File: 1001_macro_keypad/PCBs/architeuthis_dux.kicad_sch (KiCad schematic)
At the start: 18 parts, among them J1 ePaperModule, J2 RotaryModule_01, J3 RotaryModule_02, SW01 MX_SW, SW10 MX_SW, SW11 MX_SW, SW12 MX_SW, SW13 MX_SW, SW14 MX_SW, SW2 MX_SW, SW3 MX_SW, SW4 MX_SW, SW5 MX_SW, SW6 MX_SW, SW7 MX_SW, SW8 MX_SW, SW9 MX_SW, U1 Pico

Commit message: pcb modify
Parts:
- added D1: 1N4148, Diode_THT:D_DO-35_SOD27_P7.62mm_Horizontal, symbol Diode:1N4148
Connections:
- net SW6: now reaches SW6.1
- net at SW01.1: now also D1.2 (A)
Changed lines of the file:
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@@
     (stroke (width 0) (type default))
+  )
+  (global_label "SW6" (shape input) (at 57.15 73.66 90) (fields_autoplaced)
+    (effects (font (size 1.27 1.27)) (justify left))
+    (property "Intersheetrefs" "${INTERSHEET_REFS}" (at 57.15 66.8838 90)
+      (effects (font (size 1.27 1.27)) (justify left) hide)
+    )
   )
   (symbol (lib_id "Switch:SW_Push_45deg") (at 76.2 59.69 0) (unit 1)
@@
         )
       )
+    )
+  )
+  (symbol (lib_id "Diode:1N4148") (at 38.1 57.15 0) (unit 1)
+    (in_bom yes) (on_board yes) (dnp no) (fields_autoplaced)
+    (property "Reference" "D1" (at 38.1 52.07 0)
+      (effects (font (size 1.27 1.27)))
+    )
+    (property "Value" "1N4148" (at 38.1 54.61 0)
+      (effects (font (size 1.27 1.27)))
+    )
+    (property "Footprint" "Diode_THT:D_DO-35_SOD27_P7.62mm_Horizontal" (at 38.1 57.15 0)
+      (effects (font (size 1.27 1.27)) hide)
+    )
+    (property "Datasheet" "https://assets.nexperia.com/documents/data-sheet/1N4148_1N4448.pdf" (at 38.1 57.15 0)
+      (effects (font (size 1.27 1.27)) hide)
+    )
+    (property "Sim.Device" "D" (at 38.1 57.15 0)
+      (effects (font (size 1.27 1.27)) hide)
+    )
+    (property "Sim.Pins" "1=K 2=A" (at 38.1 57.15 0)
+      (effects (font (size 1.27 1.27)) hide)
+    )
+    (pin "1")
+    (pin "2")
+    (instances
+      (project "architeuthis_dux"
+        (path "/4d2fbfb9-c67d-4ccb-bbaa-2d2f4be0cbd8"
+          (reference "D1") (unit 1)
+        )
+      )

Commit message: 배션중
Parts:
- added D10, D11, D12, D13, D14, D2, D3, D4, D5, D6, D7, D8, D9: 1N4148, Diode_THT:D_DO-35_SOD27_P7.62mm_Horizontal, symbol Diode:1N4148
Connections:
- net GND: no longer SW01.2, SW10.2, SW11.2, SW12.2, SW13.2, SW14.2, SW2.2, SW3.2, SW4.2, SW5.2, SW6.2, SW7.2, SW8.2, SW9.2
- net at SW3.1: now also D3.2 (A)
- net at SW8.1: now also D8.2 (A)
- net at SW11.1: now also D11.2 (A)
- net at SW2.1: now also D2.2 (A)
- net at SW14.1: now also D14.2 (A)
- net at SW13.1: now also D13.2 (A)
- net at SW9.1: now also D9.2 (A)
- net at SW5.1: now also D5.2 (A)
- net ROW0: now reaches D1.1 (K)
- net ROW0: now also U1.1 (GPIO0), D2.1 (K), D3.1 (K), D4.1 (K)
- net COL2: now reaches U1.10 (GPIO7)
- net COL2: now also SW11.2, SW13.2, SW3.2, SW7.2
- net ROW1: now reaches U1.2 (GPIO1)
- net ROW1: now also D5.1 (K), D6.1 (K), D7.1 (K), D8.1 (K)
- net ROW2: now reaches U1.4 (GPIO2)
- net ROW2: now also D10.1 (K), D11.1 (K), D12.1 (K), D9.1 (K)
- net ROW3: now reaches U1.5 (GPIO3)
- net ROW3: now also D13.1 (K), D14.1 (K)
- net COL1: now reaches U1.6 (GPIO4)
- net COL1: now also SW10.2, SW2.2, SW6.2
- net COL0: now reaches U1.7 (GPIO5)
- net COL0: now also SW01.2, SW5.2, SW9.2
- net COL3: now reaches U1.9 (GPIO6)
- net COL3: now also SW12.2, SW14.2, SW4.2, SW8.2
- net at SW7.1: now also D7.2 (A)
- net at SW12.1: now also D12.2 (A)
- net at SW10.1: now also D10.2 (A)
- net at SW4.1: now also D4.2 (A)
- net SW6: no longer names the net of SW6.1
- net SW6: now also D6.2 (A)
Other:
- moved on the sheet: D1, SW01, SW10, SW11, SW12, SW13, SW14, SW2, SW3, SW4, SW5, SW6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

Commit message: 재배선
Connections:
- net COL0: now also SW12.2, SW4.2, SW8.2, U1.6 (GPIO4); no longer SW01.2, SW5.2, SW9.2, U1.7 (GPIO5)
- net COL1: now also SW11.2, SW3.2, SW7.2, U1.7 (GPIO5); no longer SW10.2, SW2.2, SW6.2, U1.6 (GPIO4)
- net COL2: now also SW01.2, SW14.2, SW5.2, SW9.2, U1.9 (GPIO6); no longer SW11.2, SW13.2, SW3.2, SW7.2, U1.10 (GPIO7)
- net COL3: now also SW10.2, SW13.2, SW2.2, SW6.2, U1.10 (GPIO7); no longer SW12.2, SW14.2, SW4.2, SW8.2, U1.9 (GPIO6)
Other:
- moved on the sheet: D13, D14, SW13, SW14

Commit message: ePaper
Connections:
- net GND: now also J1.7 (GND), J2.5 (GND), J3.5 (Pin_5)
- net +5V: now reaches J1.8 (VCC)
- net +5V: now also J2.1 (5V), J3.1 (Pin_1), U1.40 (VBUS)
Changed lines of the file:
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@@
+    )
+  )
+  (symbol (lib_id "power:+5V") (at 175.26 92.71 90) (unit 1)
+    (in_bom yes) (on_board yes) (dnp no) (fields_autoplaced)
+    (property "Reference" "#PWR04" (at 179.07 92.71 0)
+      (effects (font (size 1.27 1.27)) hide)
+    )
+    (property "Value" "+5V" (at 171.45 93.345 90)
+      (effects (font (size 1.27 1.27)) (justify left))
+    )
+    (property "Footprint" "" (at 175.26 92.71 0)
+      (effects (font (size 1.27 1.27)) hide)
+    )
+    (property "Datasheet" "" (at 175.26 92.71 0)
+      (effects (font (size 1.27 1.27)) hide)
+    )
+    (pin "1")
+    (instances
+      (project "architeuthis_dux"
+        (path "/4d2fbfb9-c67d-4ccb-bbaa-2d2f4be0cbd8"
+          (reference "#PWR04") (unit 1)
+        )
+      )
     )
   )
@@
     )
   )
-  (symbol (lib_id "Connector_Generic:Conn_01x05") (at 180.34 82.55 0) (unit 1)
+  (symbol (lib_name "Conn_01x05_1") (lib_id "Connector_Generic:Conn_01x05") (at 180.34 82.55 0) (unit 1)
     (in_bom yes) (on_board yes) (dnp no) (fields_autoplaced)
     (property "Reference" "J2" (at 182.88 81.915 0)
@@
     )
   )
+  (symbol (lib_id "power:GND") (at 208.28 92.71 270) (unit 1)
+    (in_bom yes) (on_board yes) (dnp no) (fields_autoplaced)
+    (property "Reference" "#PWR014" (at 201.93 92.71 0)
+      (effects (font (size 1.27 1.27)) hide)
+    )
+    (property "Value" "GND" (at 204.47 93.345 90)
+      (effects (font (size 1.27 1.27)) (justify right))
+    )
+    (property "Footprint" "" (at 208.28 92.71 0)
+      (effects (font (size 1.27 1.27)) hide)
+    )
+    (property "Datasheet" "" (at 208.28 92.71 0)
+      (effects (font (size 1.27 1.27)) hide)
+    )
+    (pin "1")
+    (instances
+      (project "architeuthis_dux"
+        (path "/4d2fbfb9-c67d-4ccb-bbaa-2d2f4be0cbd8"
+          (reference "#PWR014") (unit 1)
+        )
+      )
+    )
+  )
+  (symbol (lib_id "power:+5V") (at 175.26 77.47 90) (unit 1)
+    (in_bom yes) (on_board yes) (dnp no) (fields_autoplaced)
+    (property "Reference" "#PWR03" (at 179.07 77.47 0)
+      (effects (font (size 1.27 1.27)) hide)
+    )
+    (property "Value" "+5V" (at 171.45 78.105 90)
+      (effects (font (size 1.27 1.27)) (justify left))
+    )
+    (property "Footprint" "" (at 175.26 77.47 0)
+      (effects (font (size 1.27 1.27)) hide)
+    )
+    (property "Datasheet" "" (at 175.26 77.47 0)
+      (effects (font (size 1.27 1.27)) hide)
+    )
+    (pin "1")
+    (instances
+      (project "architeuthis_dux"
+        (path "/4d2fbfb9-c67d-4ccb-bbaa-2d2f4be0cbd8"
+          (reference "#PWR03") (unit 1)
+        )
+      )
+    )
+  )
+  (symbol (lib_id "power:GND") (at 175.26 87.63 270) (unit 1)
+    (in_bom yes) (on_board yes) (dnp no) (fields_autoplaced)
+    (property "Reference" "#PWR012" (at 168.91 87.63 0)
+      (effects (font (size 1.27 1.27)) hide)
+    )
+    (property "Value" "GND" (at 171.45 88.265 90)
+      (effects (font (size 1.27 1.27)) (justify right))
+    )
+    (property "Footprint" "" (at 175.26 87.63 0)
+      (effects (font (size 1.27 1.27)) hide)
+    )
+    (property "Datasheet" "" (at 175.26 87.63 0)
+      (effects (font (size 1.27 1.27)) hide)
+    )
+    (pin "1")
+    (instances
+      (project "architeuthis_dux"
+        (path "/4d2fbfb9-c67d-4ccb-bbaa-2d2f4be0cbd8"
+          (reference "#PWR012") (unit 1)
+        )
+      )
+    )
+  )
   (symbol (lib_id "Switch:SW_Push_45deg") (at 35.56 91.44 0) (unit 1)
     (in_bom yes) (on_board yes) (dnp no) (fields_autoplaced)
@@
         (path "/4d2fbfb9-c67d-4ccb-bbaa-2d2f4be0cbd8"
           (reference "D1") (unit 1)
+        )
+      )
+    )
+  )
+  (symbol (lib_id "power:+5V") (at 151.13 41.91 270) (unit 1)
+    (in_bom yes) (on_board yes) (dnp no) (fields_autoplaced)
+    (property "Reference" "#PWR01" (at 147.32 41.91 0)
+      (effects (font (size 1.27 1.27)) hide)
+    )
+    (property "Value" "+5V" (at 154.94 42.545 90)
+      (effects (font (size 1.27 1.27)) (justify left))
+    )
+    (property "Footprint" "" (at 151.13 41.91 0)
+      (effects (font (size 1.27 1.27)) hide)
+    )
+    (property "Datasheet" "" (at 151.13 41.91 0)
+      (effects (font (size 1.27 1.27)) hide)
+    )
+    (pin "1")
+    (instances
+      (project "architeuthis_dux"
+        (path "/4d2fbfb9-c67d-4ccb-bbaa-2d2f4be0cbd8"
+          (reference "#PWR01") (unit 1)
         )
       )
@@
     )
   )
+  (symbol (lib_id "power:GND") (at 175.26 102.87 270) (unit 1)
+    (in_bom yes) (on_board yes) (dnp no) (fields_autoplaced)
+    (property "Reference" "#PWR013" (at 168.91 102.87 0)
+      (effects (font (size 1.27 1.27)) hide)
+    )
+    (property "Value" "GND" (at 171.45 103.505 90)
+      (effects (font (size 1.27 1.27)) (justify right))
+    )
+    (property "Footprint" "" (at 175.26 102.87 0)
+      (effects (font (size 1.27 1.27)) hide)
+    )
+    (property "Datasheet" "" (at 175.26 102.87 0)
+      (effects (font (size 1.27 1.27)) hide)
+    )
+    (pin "1")
+    (instances
+      (project "architeuthis_dux"
+        (path "/4d2fbfb9-c67d-4ccb-bbaa-2d2f4be0cbd8"
+          (reference "#PWR013") (unit 1)
+        )
+      )
+    )
+  )
   (symbol (lib_id "power:GND") (at 151.13 46.99 90) (unit 1)
     (in_bom yes) (on_board yes) (dnp no) (fields_autoplaced)
@@
         )
       )
+    )
+  )
+  (symbol (lib_id "power:+5V") (at 208.28 95.25 90) (unit 1)
+    (in_bom yes) (on_board yes) (dnp no) (fields_autoplaced)
+    (property "Reference" "#PWR02" (at 212.09 95.25 0)
+      (effects (font (size 1.27 1.27)) hide)
+    )
+    (property "Value" "+5V" (at 204.47 95.885 90)
+      (effects (font (size 1.27 1.27)) (justify left))
+    )
+    (property "Footprint" "" (at 208.28 95.25 0)
+      (effects (font (size 1.27 1.27)) hide)
+    )
+    (property "Datasheet" "" (at 208.28 95.25 0)
+      (effects (font (size 1.27 1.27)) hide)
+    )
+    (pin "1")
+    (instances
+      (project "architeuthis_dux"
+        (path "/4d2fbfb9-c67d-4ccb-bbaa-2d2f4be0cbd8"
+          (reference "#PWR02") (unit 1)
+        )
+      )

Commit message: 일부수정
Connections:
- net +5V: now also J1.1 (BUSY); no longer J1.8 (VCC)
- net GND: now also J1.2 (RES); no longer J1.7 (GND)
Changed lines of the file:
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@@
     )
   )
-  (symbol (lib_id "power:GND") (at 208.28 92.71 270) (unit 1)
-    (in_bom yes) (on_board yes) (dnp no) (fields_autoplaced)
-    (property "Reference" "#PWR014" (at 201.93 92.71 0)
-      (effects (font (size 1.27 1.27)) hide)
-    )
-    (property "Value" "GND" (at 204.47 93.345 90)
+  (symbol (lib_id "power:GND") (at 208.28 80.01 270) (unit 1)
+    (in_bom yes) (on_board yes) (dnp no) (fields_autoplaced)
+    (property "Reference" "#PWR014" (at 201.93 80.01 0)
+      (effects (font (size 1.27 1.27)) hide)
+    )
+    (property "Value" "GND" (at 204.47 80.645 90)
       (effects (font (size 1.27 1.27)) (justify right))
     )
-    (property "Footprint" "" (at 208.28 92.71 0)
-      (effects (font (size 1.27 1.27)) hide)
-    )
-    (property "Datasheet" "" (at 208.28 92.71 0)
+    (property "Footprint" "" (at 208.28 80.01 0)
+      (effects (font (size 1.27 1.27)) hide)
+    )
+    (property "Datasheet" "" (at 208.28 80.01 0)
       (effects (font (size 1.27 1.27)) hide)
     )
@@
     )
   )
-  (symbol (lib_id "power:+5V") (at 208.28 95.25 90) (unit 1)
-    (in_bom yes) (on_board yes) (dnp no) (fields_autoplaced)
-    (property "Reference" "#PWR02" (at 212.09 95.25 0)
-      (effects (font (size 1.27 1.27)) hide)
-    )
-    (property "Value" "+5V" (at 204.47 95.885 90)
-      (effects (font (size 1.27 1.27)) (justify left))
-    )
-    (property "Footprint" "" (at 208.28 95.25 0)
-      (effects (font (size 1.27 1.27)) hide)
-    )
-    (property "Datasheet" "" (at 208.28 95.25 0)
-      (effects (font (size 1.27 1.27)) hide)
-    )
+  (symbol (lib_id "power:+5V") (at 208.28 77.47 90) (unit 1)
+    (in_bom yes) (on_board yes) (dnp no) (fields_autoplaced)
+    (property "Reference" "#PWR02" (at 212.09 77.47 0)
+      (effects (font (size 1.27 1.27)) hide)
+    )
+    (property "Value" "+5V" (at 204.47 78.105 90)
+      (effects (font (size 1.27 1.27)) (justify left))
+    )
+    (property "Footprint" "" (at 208.28 77.47 0)
+      (effects (font (size 1.27 1.27)) hide)
+    )
+    (property "Datasheet" "" (at 208.28 77.47 0)
+      (effects (font (size 1.27 1.27)) hide)
+    )

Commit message: 배선작업 거의 완료
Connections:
- net at J1.3 (D/C): now also U1.34 (GPIO28_ADC2)
- net at J1.4 (CS): now also U1.26 (GPIO20)
- net at J1.5 (SCL): now also U1.32 (GPIO27_ADC1)
- net at J1.6 (SDA): now also U1.27 (GPIO21)
- net at J1.7 (GND): now also U1.31 (GPIO26_ADC0)
- net at J1.8 (VCC): now also U1.29 (GPIO22)
- net at J2.2 (KEY): now also U1.25 (GPIO19)
- net at J2.3 (S2): now also U1.24 (GPIO18)
- net at J2.4 (S1): now also U1.22 (GPIO17)
- net at J3.2 (Pin_2): now also U1.21 (GPIO16)
- net at J3.3 (Pin_3): now also U1.19 (GPIO14)
- net at J3.4 (Pin_4): now also U1.20 (GPIO15)
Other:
- moved on the sheet: J2, J3

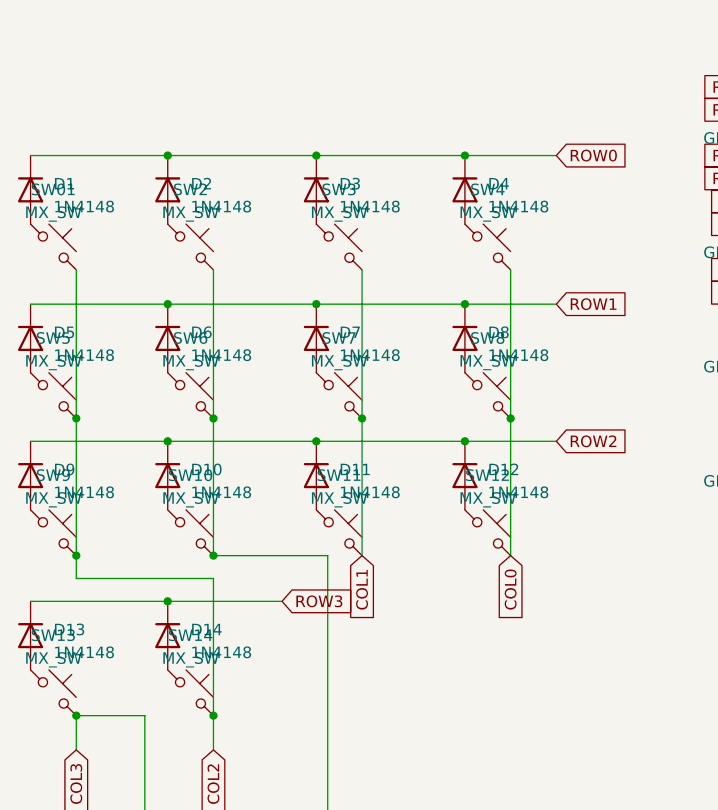
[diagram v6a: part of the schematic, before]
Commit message: 펌웨어 추가, 다이오드 방향 변경 및 재배선
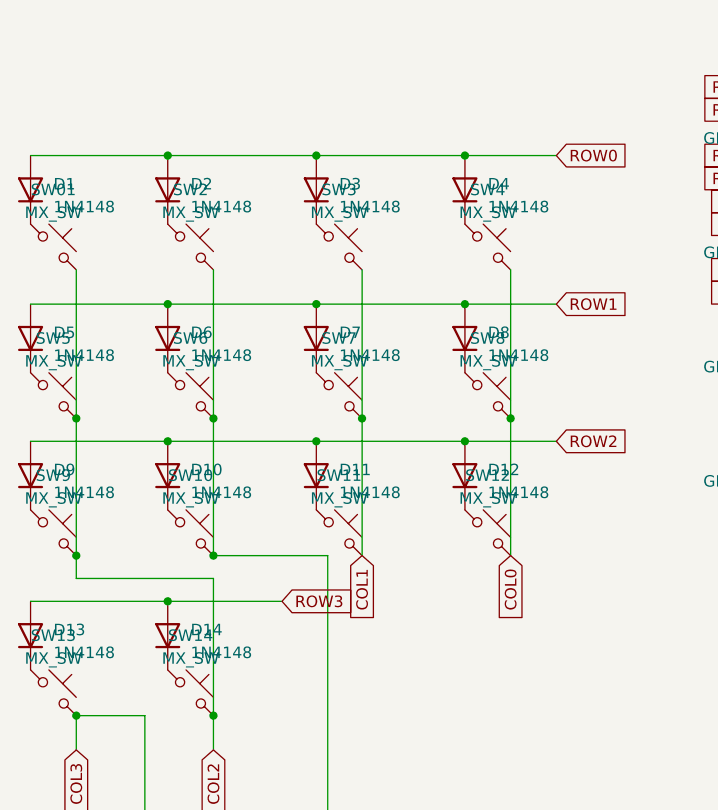
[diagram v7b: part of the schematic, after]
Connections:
- net ROW0: now also D1.2 (A), D2.2 (A), D3.2 (A), D4.2 (A); no longer D1.1 (K), D2.1 (K), D3.1 (K), D4.1 (K)
- net ROW1: now also D5.2 (A), D6.2 (A), D7.2 (A), D8.2 (A); no longer D5.1 (K), D6.1 (K), D7.1 (K), D8.1 (K)
- net ROW2: now also D10.2 (A), D11.2 (A), D12.2 (A), D9.2 (A); no longer D10.1 (K), D11.1 (K), D12.1 (K), D9.1 (K)
- net ROW3: now also D13.2 (A), D14.2 (A); no longer D13.1 (K), D14.1 (K)
- net at SW3.1: now also D3.1 (K); no longer D3.2 (A)
- net at SW8.1: now also D8.1 (K); no longer D8.2 (A)
- net at SW13.1: now also D13.1 (K); no longer D13.2 (A)
- net at SW4.1: now also D4.1 (K); no longer D4.2 (A)
- net at SW6.1: now also D6.1 (K); no longer D6.2 (A)
- net at SW11.1: now also D11.1 (K); no longer D11.2 (A)
- net at SW5.1: now also D5.1 (K); no longer D5.2 (A)
- net at SW2.1: now also D2.1 (K); no longer D2.2 (A)
- net at SW14.1: now also D14.1 (K); no longer D14.2 (A)
- net at SW9.1: now also D9.1 (K); no longer D9.2 (A)
- net at SW01.1: now also D1.1 (K); no longer D1.2 (A)
- net at SW12.1: now also D12.1 (K); no longer D12.2 (A)
- net at SW7.1: now also D7.1 (K); no longer D7.2 (A)
- net at SW10.1: now also D10.1 (K); no longer D10.2 (A)
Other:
- moved on the sheet: D1, D10, D11, D12, D13, D14, D2, D3, D4, D5, D6, D7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

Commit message: 디스플레이 및 로터리 관련
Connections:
- net +5V: now also U1.36 (3V3); no longer U1.40 (VBUS)
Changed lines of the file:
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@@
     )
   )
-  (symbol (lib_id "power:+5V") (at 151.13 41.91 270) (unit 1)
+  (symbol (lib_id "power:+5V") (at 151.13 52.07 270) (unit 1)
     (in_bom yes) (on_board yes) (dnp no) (fields_autoplaced)
-    (property "Reference" "#PWR01" (at 147.32 41.91 0)
+    (property "Reference" "#PWR01" (at 147.32 52.07 0)
       (effects (font (size 1.27 1.27)) hide)
     )
-    (property "Value" "+5V" (at 154.94 42.545 90)
+    (property "Value" "+5V" (at 154.94 52.705 90)
       (effects (font (size 1.27 1.27)) (justify left))
     )
-    (property "Footprint" "" (at 151.13 41.91 0)
+    (property "Footprint" "" (at 151.13 52.07 0)
       (effects (font (size 1.27 1.27)) hide)
     )
-    (property "Datasheet" "" (at 151.13 41.91 0)
+    (property "Datasheet" "" (at 151.13 52.07 0)
       (effects (font (size 1.27 1.27)) hide)
     )
